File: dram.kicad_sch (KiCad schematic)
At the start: 21 parts, among them K9 4164

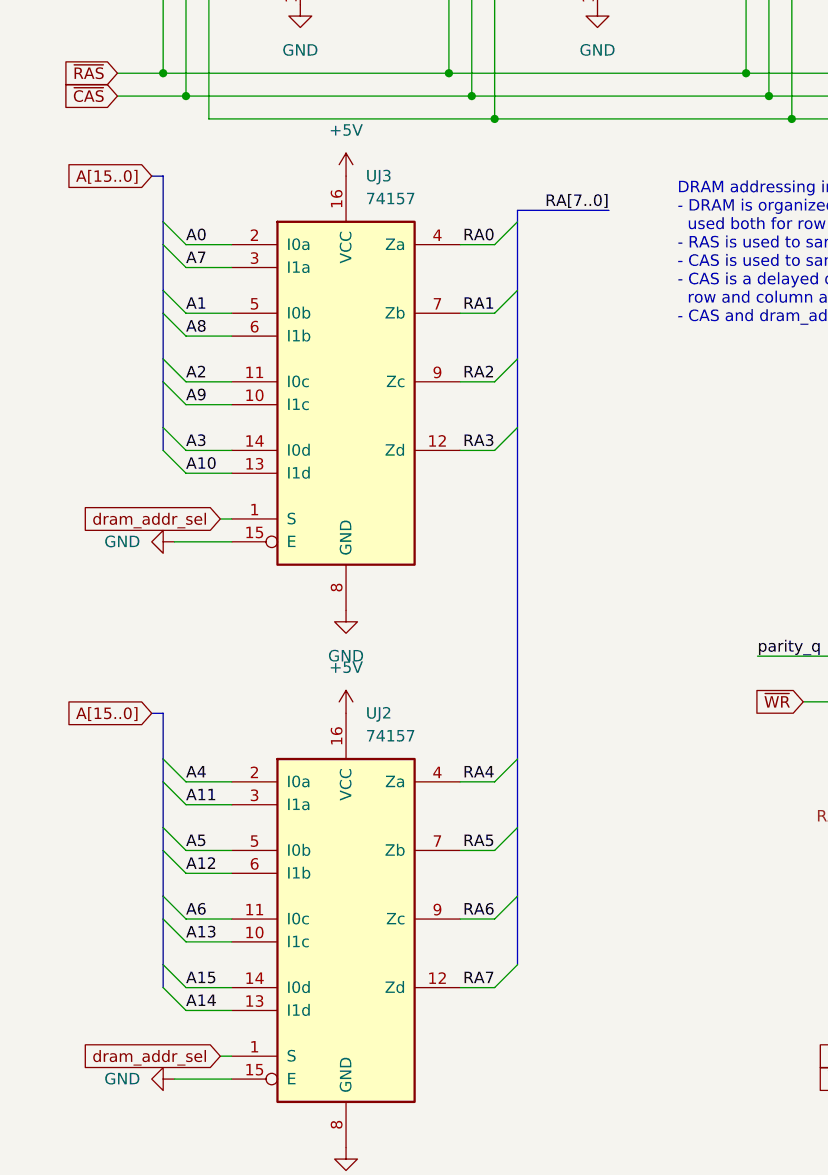
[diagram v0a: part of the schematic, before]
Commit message: Fixed missing resistors in dram addresses
TODO: check their values on the actual PCB
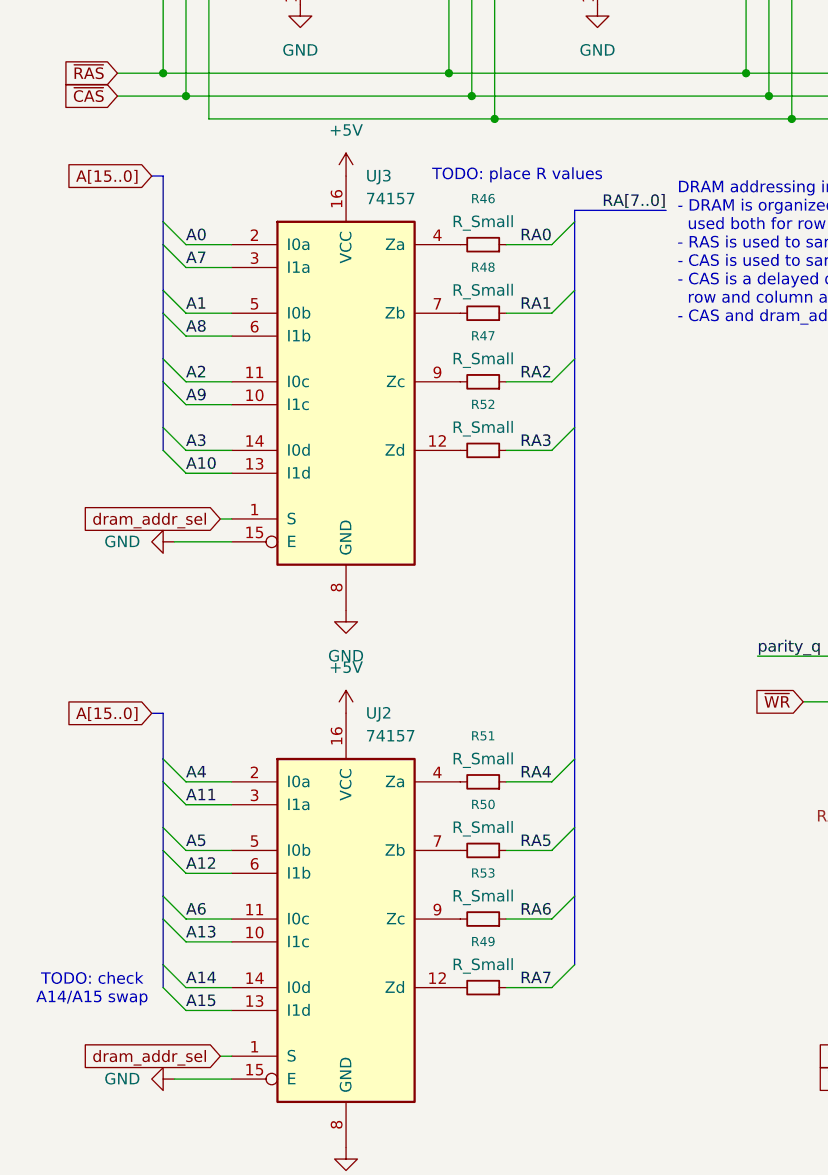
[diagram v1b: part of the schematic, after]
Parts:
- added R46, R47, R48, R49, R50, R51, R52, R53: R_Small, Resistor_THT:R_Axial_DIN0204_L3.6mm_D1.6mm_P5.08mm_Vertical, symbol Device:R_Small
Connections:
- net A14: now also UJ2.14 (I0d); no longer UJ2.13 (I1d)
- net A15: now also UJ2.13 (I1d); no longer UJ2.14 (I0d)
- net RA0: now also R46.1; no longer UJ3.4 (Za)
- net RA1: now also R48.1; no longer UJ3.7 (Zb)
- net RA2: now also R47.1; no longer UJ3.9 (Zc)
- net RA3: now also R52.1; no longer UJ3.12 (Zd)
- net RA4: now also R51.1; no longer UJ2.4 (Za)
- net RA5: now also R50.1; no longer UJ2.7 (Zb)
- net RA6: now also R53.1; no longer UJ2.9 (Zc)
- net RA7: now also R49.1; no longer UJ2.12 (Zd)
- new net: R49.2, UJ2.12 (Zd)
- new net: R51.2, UJ2.4 (Za)
- new net: R50.2, UJ2.7 (Zb)
- new net: R53.2, UJ2.9 (Zc)
- new net: R47.2, UJ3.9 (Zc)
- new net: R52.2, UJ3.12 (Zd)
- new net: R46.2, UJ3.4 (Za)
- new net: R48.2, UJ3.7 (Zb)
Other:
- note added: "TODO: check A14/A15 swap"
- note added: "TODO: place R values"

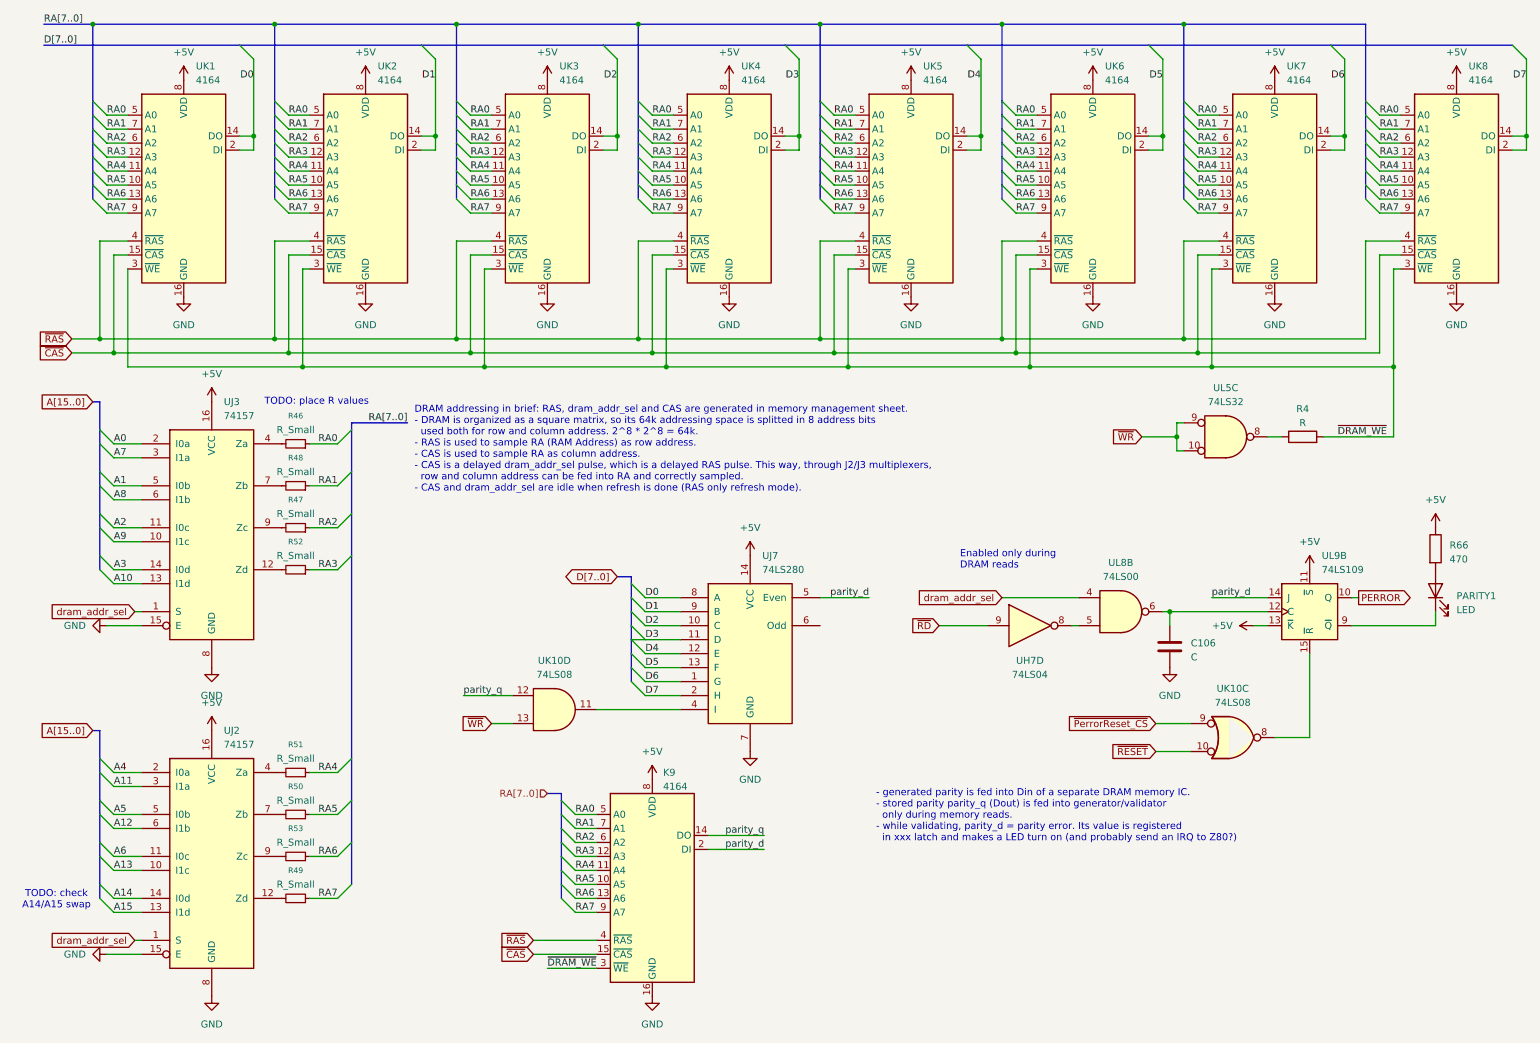
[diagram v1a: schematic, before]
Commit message: pcb: added and placed almost all components
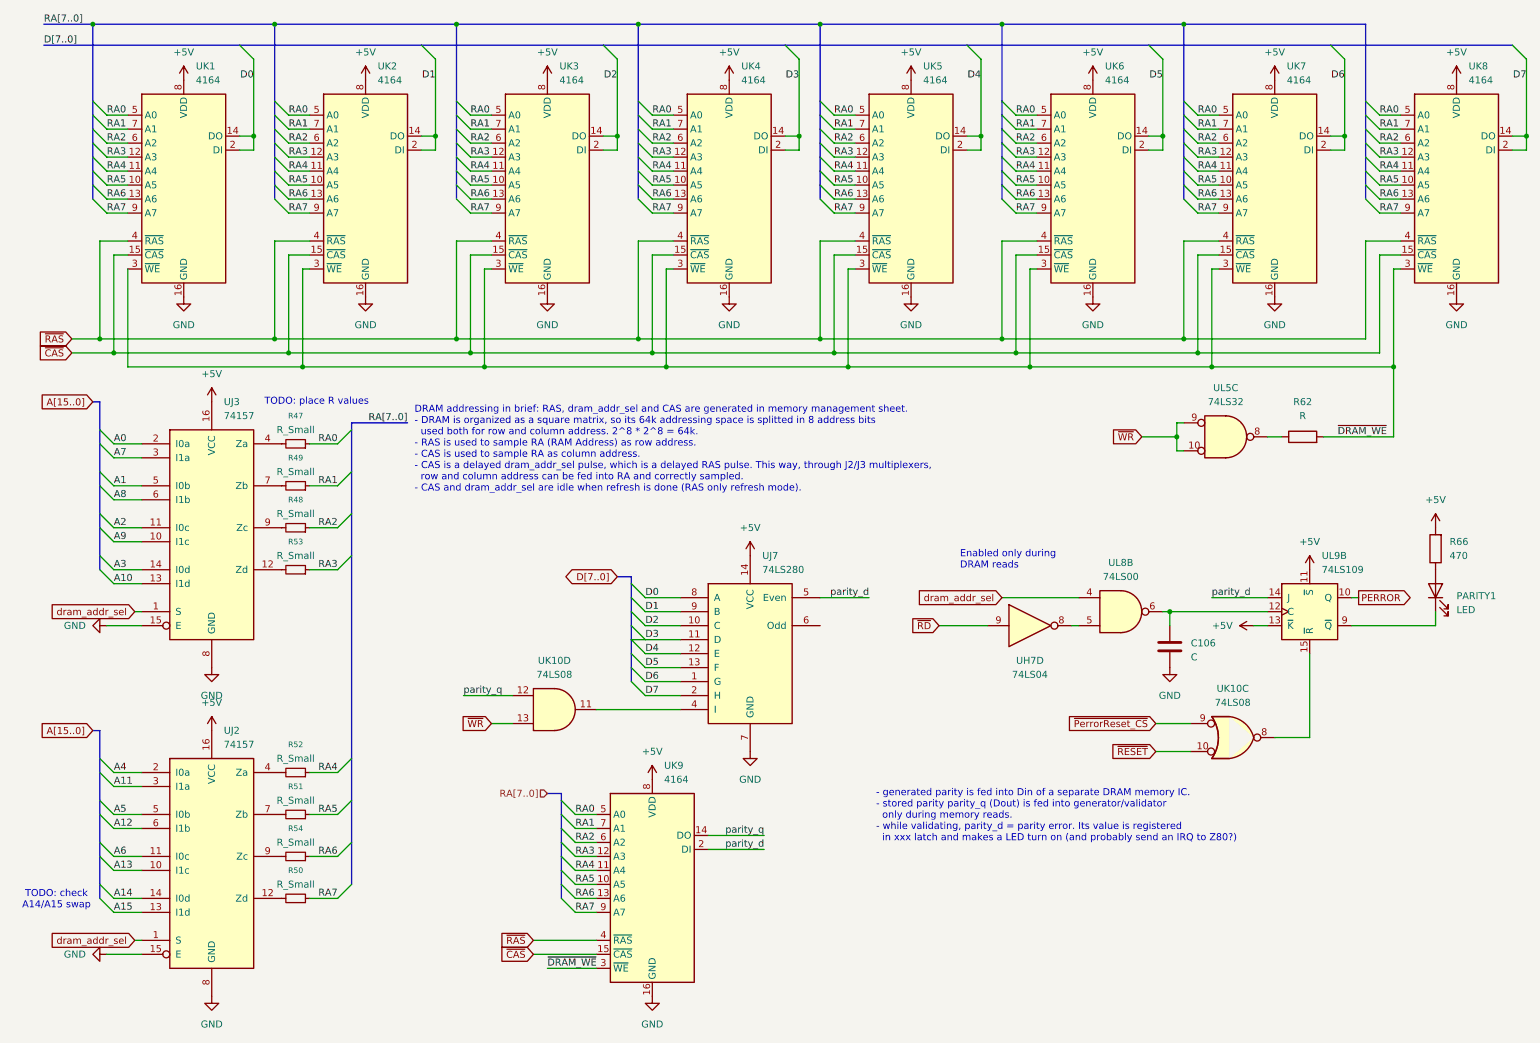
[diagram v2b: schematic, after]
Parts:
- C106: footprint (none) -> Capacitor_THT:C_Disc_D4.3mm_W1.9mm_P5.00mm
- PARITY1: footprint (none) -> LED_THT:LED_D3.0mm
- R62: renamed from R4; footprint (none) -> Resistor_THT:R_Axial_DIN0204_L3.6mm_D1.6mm_P5.08mm_Vertical
- R66: footprint (none) -> Resistor_THT:R_Axial_DIN0204_L3.6mm_D1.6mm_P5.08mm_Vertical
- renumbered R46 to R47, R47 to R48, R48 to R49, R49 to R50, R50 to R51, R51 to R52, R52 to R53, R53 to R54, K9 to UK9
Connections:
- net +5V: now also R66.2; no longer R66.1
- net at PARITY1.2 (A): now also R66.1; no longer R66.2
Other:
- moved on the sheet: R66
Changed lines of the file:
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@@
 		(dnp no)
 		(fields_autoplaced yes)
-		(property "Reference" "K9"
-			(at 126.4159 151.13 0)
+		(property "Reference" "UK9"
+			(at 126.6033 149.86 0)
 			(effects
 				(font
@@
 		)
 		(property "Value" "4164"
-			(at 126.4159 153.67 0)
+			(at 126.6033 152.4 0)
 			(effects
 				(font
@@
 			(project "ceda"
 				(path "/12a6dbe3-008d-4c5b-88f6-9f1c816060be/f05e0b09-5f96-4638-8985-dbb50d0f6ef2"
-					(reference "K9")
+					(reference "UK9")
 					(unit 1)
 				)
@@
 		(dnp no)
 		(fields_autoplaced yes)
-		(property "Reference" "R47"
+		(property "Reference" "R48"
 			(at 59.69 101.6 90)
 			(effects
@@
 			(project "ceda"
 				(path "/12a6dbe3-008d-4c5b-88f6-9f1c816060be/f05e0b09-5f96-4638-8985-dbb50d0f6ef2"
-					(reference "R47")
+					(reference "R48")
 					(unit 1)
 				)
@@
 		(dnp no)
 		(fields_autoplaced yes)
-		(property "Reference" "R49"
+		(property "Reference" "R50"
 			(at 59.69 168.91 90)
 			(effects
@@
 			(project "ceda"
 				(path "/12a6dbe3-008d-4c5b-88f6-9f1c816060be/f05e0b09-5f96-4638-8985-dbb50d0f6ef2"
-					(reference "R49")
+					(reference "R50")
 					(unit 1)
 				)
@@
 			)
 		)
-		(property "Footprint" ""
+		(property "Footprint" "Capacitor_THT:C_Disc_D4.3mm_W1.9mm_P5.00mm"
 			(at 219.4052 132.08 0)
 			(effects
@@
 	(symbol
 		(lib_id "Device:R")
-		(at 266.7 110.49 0)
+		(at 266.7 110.49 180)
 		(unit 1)
 		(exclude_from_sim no)
@@
 		(fields_autoplaced yes)
 		(property "Reference" "R66"
-			(at 269.24 109.855 0)
+			(at 269.24 109.2199 0)
 			(effects
 				(font
 					(size 1.27 1.27)
 				)
-				(justify left)
+				(justify right)
 			)
 		)
 		(property "Value" "470"
-			(at 269.24 112.395 0)
+			(at 269.24 111.7599 0)
 			(effects
 				(font
 					(size 1.27 1.27)
 				)
-				(justify left)
+				(justify right)
 			)
 		)
-		(property "Footprint" ""
-			(at 264.922 110.49 90)
+		(property "Footprint" "Resistor_THT:R_Axial_DIN0204_L3.6mm_D1.6mm_P5.08mm_Vertical"
+			(at 268.478 110.49 90)
 			(effects
 				(font
@@
 		(dnp no)
 		(fields_autoplaced yes)
-		(property "Reference" "R52"
+		(property "Reference" "R53"
 			(at 59.69 109.22 90)
 			(effects
@@
 			(project "ceda"
 				(path "/12a6dbe3-008d-4c5b-88f6-9f1c816060be/f05e0b09-5f96-4638-8985-dbb50d0f6ef2"
-					(reference "R52")
+					(reference "R53")
 					(unit 1)
 				)
@@
 		(dnp no)
 		(fields_autoplaced yes)
-		(property "Reference" "R50"
+		(property "Reference" "R51"
 			(at 59.69 153.67 90)
 			(effects
@@
 			(project "ceda"
 				(path "/12a6dbe3-008d-4c5b-88f6-9f1c816060be/f05e0b09-5f96-4638-8985-dbb50d0f6ef2"
-					(reference "R50")
+					(reference "R51")
 					(unit 1)
 				)
@@
 		(dnp no)
 		(fields_autoplaced yes)
-		(property "Reference" "R46"
+		(property "Reference" "R47"
 			(at 59.69 86.36 90)
 			(effects
@@
 			(project ""
 				(path "/12a6dbe3-008d-4c5b-88f6-9f1c816060be/f05e0b09-5f96-4638-8985-dbb50d0f6ef2"
-					(reference "R46")
+					(reference "R47")
 					(unit 1)
 				)
@@
 		(dnp no)
 		(fields_autoplaced yes)
-		(property "Reference" "R4"
-			(at 242.57 85.09 90)
+		(property "Reference" "R62"
+			(at 242.57 83.82 90)
 			(effects
 				(font
@@
 		)
 		(property "Value" "R"
-			(at 242.57 87.63 90)
+			(at 242.57 86.36 90)
 			(effects
 				(font
@@
 			)
 		)
-		(property "Footprint" ""
+		(property "Footprint" "Resistor_THT:R_Axial_DIN0204_L3.6mm_D1.6mm_P5.08mm_Vertical"
 			(at 242.57 91.948 90)
 			(effects
@@
 			(project "ceda"
 				(path "/12a6dbe3-008d-4c5b-88f6-9f1c816060be/f05e0b09-5f96-4638-8985-dbb50d0f6ef2"
-					(reference "R4")
+					(reference "R62")
 					(unit 1)
 				)
@@
 			)
 		)
-		(property "Footprint" ""
+		(property "Footprint" "LED_THT:LED_D3.0mm"
 			(at 266.7 118.11 0)
 			(effects
@@
 		(dnp no)
 		(fields_autoplaced yes)
-		(property "Reference" "R53"
+		(property "Reference" "R54"
 			(at 59.69 161.29 90)
 			(effects
@@
 			(project "ceda"
 				(path "/12a6dbe3-008d-4c5b-88f6-9f1c816060be/f05e0b09-5f96-4638-8985-dbb50d0f6ef2"
-					(reference "R53")
+					(reference "R54")
 					(unit 1)
 				)
@@
 		(dnp no)
 		(fields_autoplaced yes)
-		(property "Reference" "R48"
+		(property "Reference" "R49"
 			(at 59.69 93.98 90)
 			(effects
@@
 			(project "ceda"
 				(path "/12a6dbe3-008d-4c5b-88f6-9f1c816060be/f05e0b09-5f96-4638-8985-dbb50d0f6ef2"
-					(reference "R48")
+					(reference "R49")
 					(unit 1)
 				)
@@
 		(dnp no)
 		(fields_autoplaced yes)
-		(property "Reference" "R51"
+		(property "Reference" "R52"
 			(at 59.69 146.05 90)
 			(effects
@@
 			(project "ceda"
 				(path "/12a6dbe3-008d-4c5b-88f6-9f1c816060be/f05e0b09-5f96-4638-8985-dbb50d0f6ef2"
-					(reference "R51")
+					(reference "R52")
 					(unit 1)
 				)

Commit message: pcb: added power in caps, reordered ref no, fixed power traces
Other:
- note removed: "TODO: check A14/A15 swap"
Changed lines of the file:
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@@
-		)
-	)
-	(text "TODO: check\nA14/A15 swap"
-		(exclude_from_sim no)
-		(at 16.256 174.244 0)
-		(effects
-			(font
-				(size 1.27 1.27)
-			)
 		)
 	)
